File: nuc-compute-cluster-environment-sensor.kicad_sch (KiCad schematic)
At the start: 112 parts, among them J1 USB4105-GF-A, J2 SM04B-SRSS-TB-LF-SN, J3 SM04B-SRSS-TB-LF-SN, U1 FT4232H-56Q, U2 AP7370-33SA-7, U3 STM32G474CET6, U4 MB85RC1MTPNF-G, U5 SHT45, U6 BME280, Y1 ABM3B-12.000MHZ-B2-T, Y2 ECS-_327-12_5-34B-TR, Y3 ABM3B-8.000MHZ-10-1-U-T

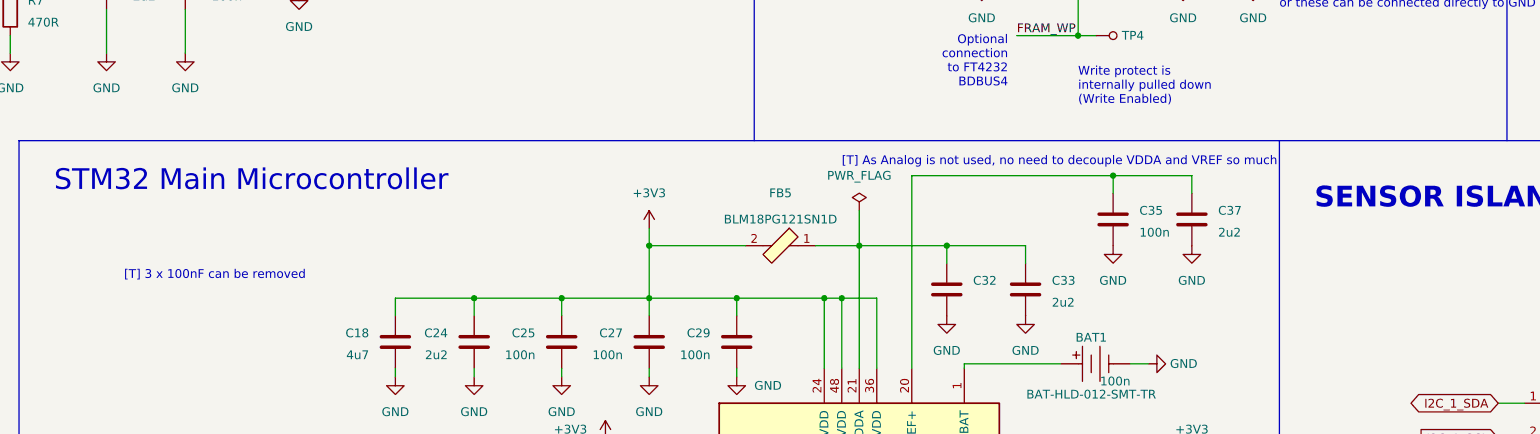
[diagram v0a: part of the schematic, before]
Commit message: Started to route signals to closest passive components to seek for possible placement optimization
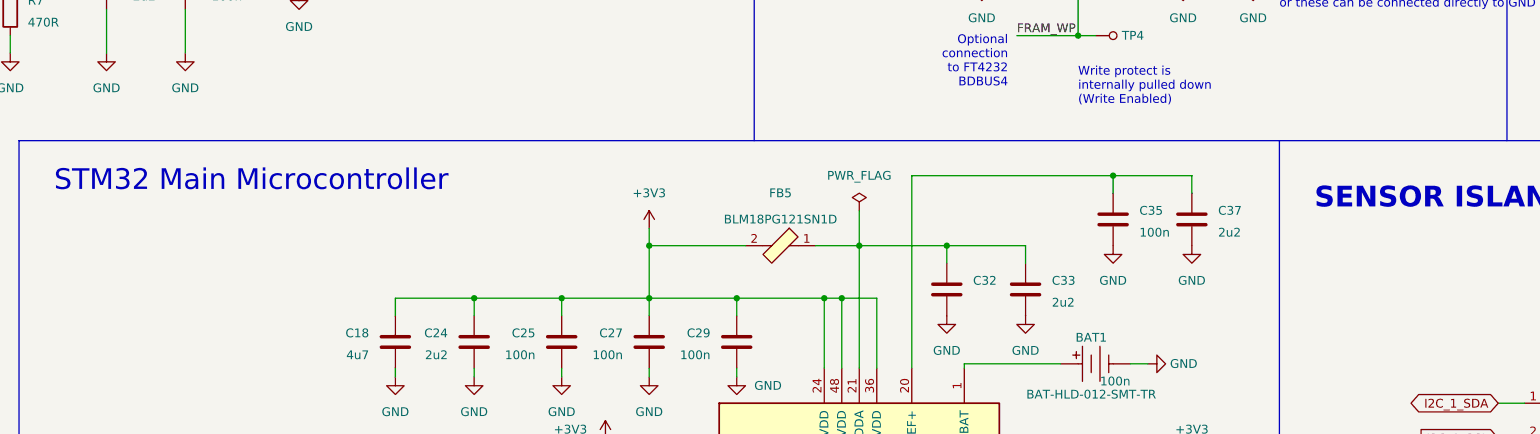
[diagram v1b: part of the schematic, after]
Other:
- note removed: "[T] 3 x 100nF can be removed"
- note removed: "[T] As Analog is not used, no need to decouple VDDA and VREF so much"

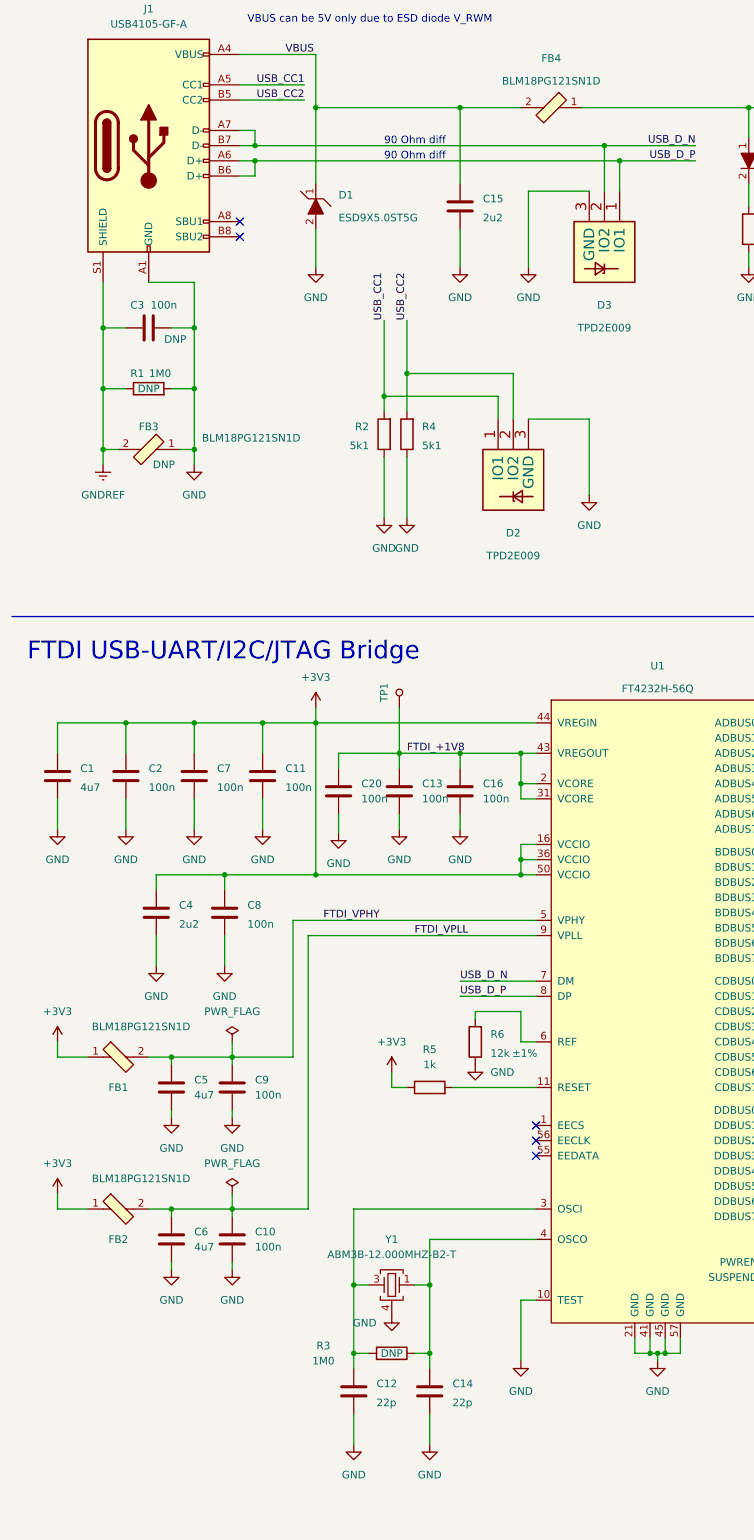
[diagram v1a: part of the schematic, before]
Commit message: Another iteration of component placements, initial routing of signals
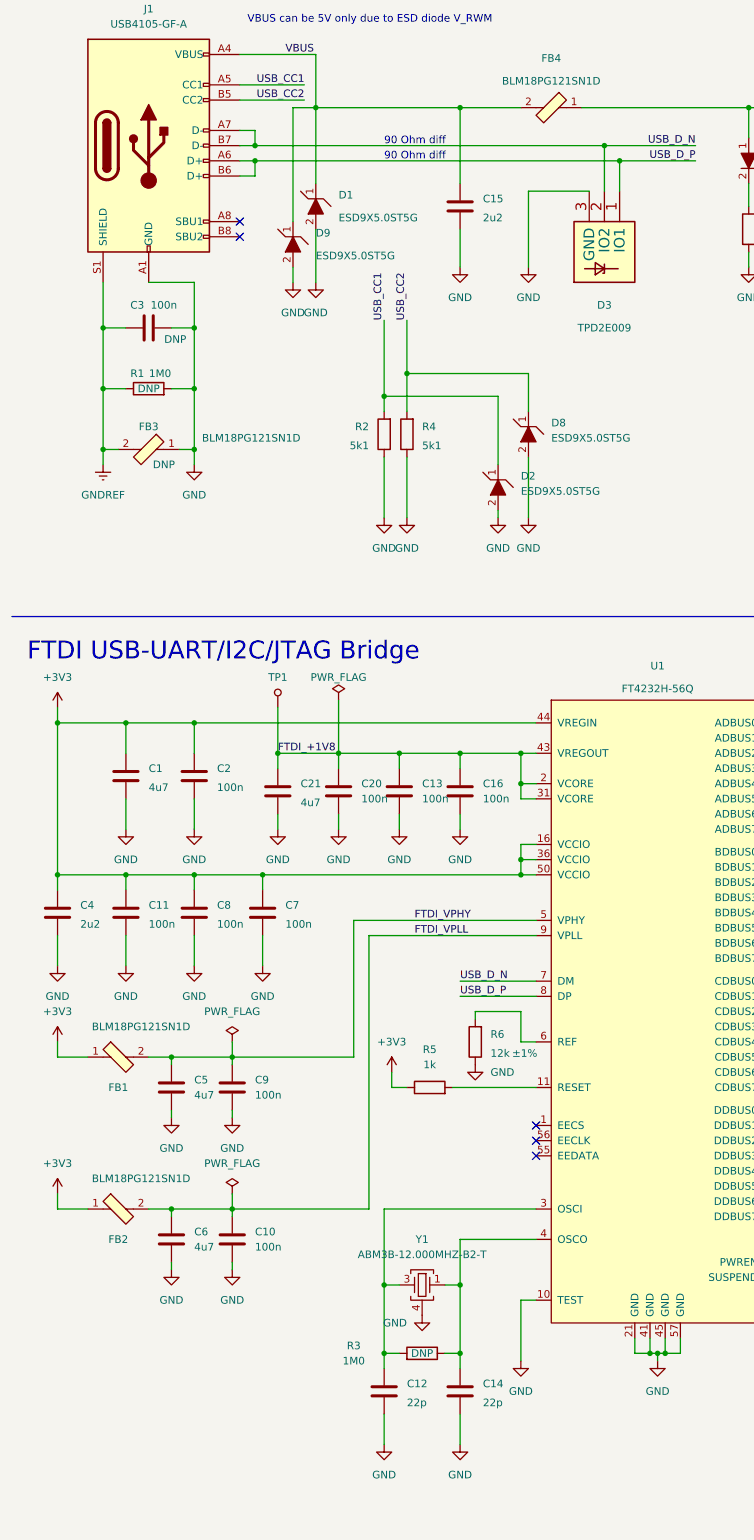
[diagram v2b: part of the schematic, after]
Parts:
- removed D2: TPD2E009, antmicro-footprints:SOT-723, symbol antmicroTVSDiodes:TPD2E009
- added C21: C_4u7_0402, antmicro-footprints:0402-cap, symbol antmicroCapacitors0402:C_4u7_0402
- added D2, D8, D9: ESD9X5.0ST5G, antmicro-footprints:SOD-923, symbol antmicroTVSDiodes:ESD9X5.0ST5G
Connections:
- net FTDI_+1V8: now also C21.1
- net GND: now also C21.2, D2.2, D8.2, D9.2
- net USB_CC1: now also D2.1
- net USB_CC2: now also D8.1
- net VBUS: now also D9.1
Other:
- moved on the sheet: C1, C11, C12, C14, C2, C4, C7, C8, R3, TP1, Y1

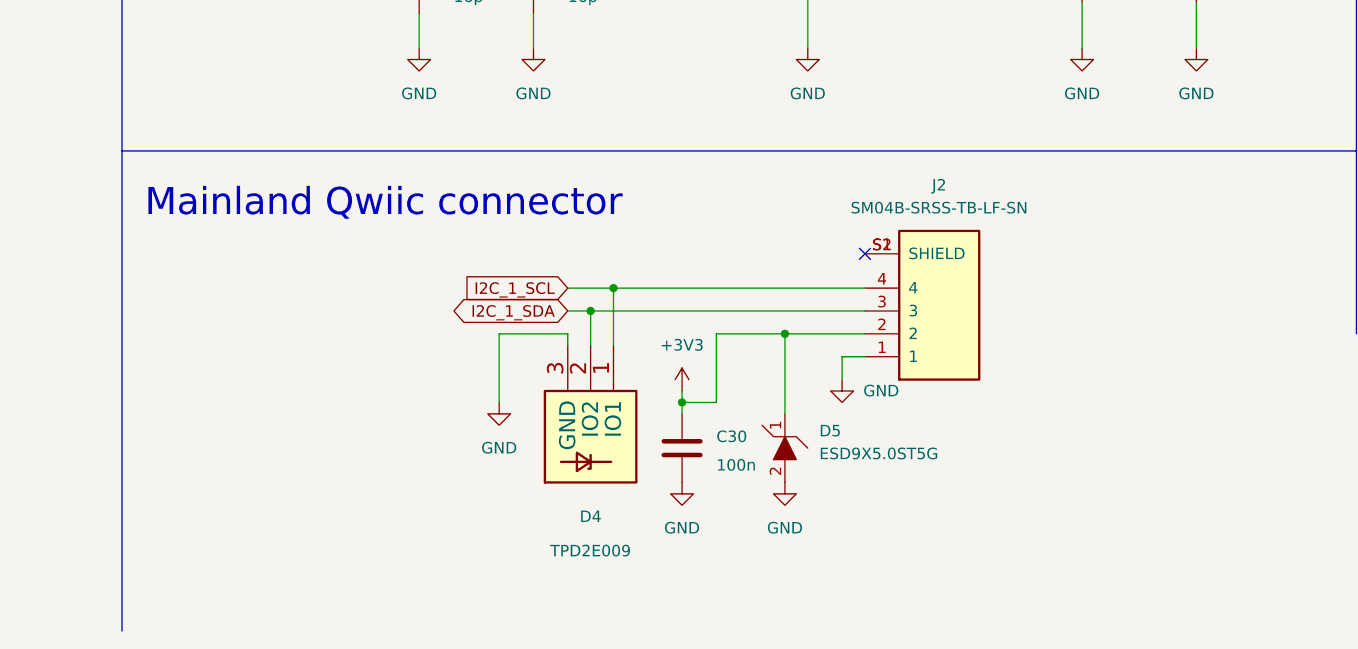
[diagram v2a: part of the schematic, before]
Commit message: Added mounting holes and changed PCB size to 50x30mm
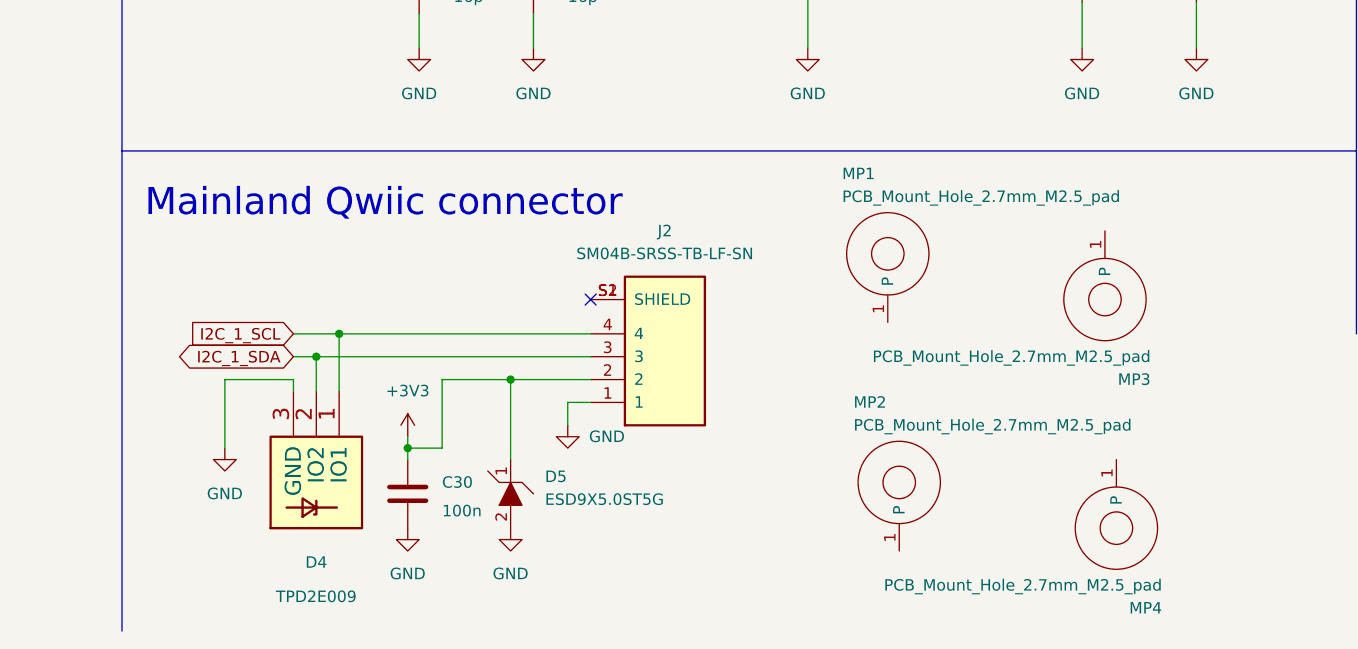
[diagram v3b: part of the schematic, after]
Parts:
- added MP1, MP2, MP3, MP4: PCB_Mount_Hole_2.7mm_M2.5_pad, antmicro-footprints:mounting-hole-2.7mm-M2.5-Pad, symbol antmicroMechanicalParts:PCB_Mount_Hole_2.7mm_M2.5_pad
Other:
- moved on the sheet: C30, D4, D5, J2

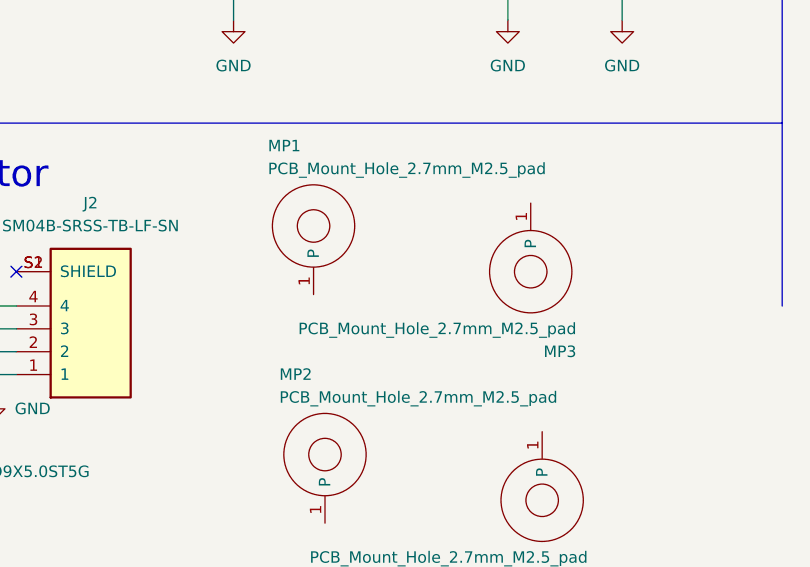
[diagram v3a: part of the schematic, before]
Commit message: New component placement after review, all components moved to top layer except battery and connector
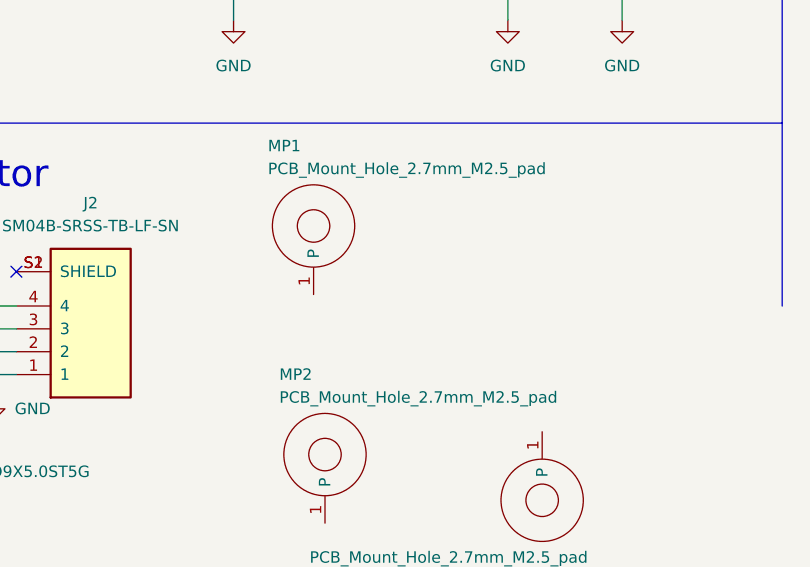
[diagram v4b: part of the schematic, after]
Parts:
- removed MP3: PCB_Mount_Hole_2.7mm_M2.5_pad, antmicro-footprints:mounting-hole-2.7mm-M2.5-Pad, symbol antmicroMechanicalParts:PCB_Mount_Hole_2.7mm_M2.5_pad

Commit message: Added 1k pullup on FRAM write protection pin, 470R serial resistors added on SWDIO and SWCLK, keepout zones for GND added around USB
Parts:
- added R10, R9: R_470R_0402, antmicro-footprints:0402-res, symbol antmicroResistors0402:R_470R_0402
- added R27: R_1k_0402, antmicro-footprints:0402-res, symbol antmicroResistors0402:R_100k_0402
- renumbered C4 to C1, C7 to C11, C21 to C12, C20 to C13, C12 to C14, C13 to C15, C15 to C16, C16 to C17, C14 to C18, C17 to C19, C1 to C2, C19 to C20, C18 to C21, C23 to C22, C24 to C23, C30 to C24, C11 to C3, C31 to C30, C32 to C31, C33 to C32, C34 to C33, C35 to C34, C36 to C35, C37 to C36, C38 to C37, C39 to C38, C40 to C39, C3 to C4, C41 to C40, C2 to C7, D9 to D1, D1 to D2, D2 to D3, D8 to D4, D3 to D5, D4 to D6, D5 to D7, D6 to D8, D7 to D9, MP4 to MP3, R9 to R11, R10 to R12, R11 to R13, R12 to R14, R13 to R15, R14 to R16, R15 to R17, R16 to R18, R17 to R19, R18 to R20, R19 to R21, R20 to R22, R21 to R23, R22 to R24, R23 to R25, R24 to R26, R25 to R28, R26 to R29, R4 to R3, R27 to R30, R28 to R31, R29 to R32, R30 to R33, R31 to R34, R32 to R35, R33 to R36, R34 to R37, R35 to R38, R36 to R39, R3 to R4, R37 to R40
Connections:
- net +3V3: now also R27.2
- net FRAM_WP: now also R27.1
- net SWCLK-JTCK: now also R9.1; no longer U1.12 (ADBUS0)
- net SWDIO-JTMS: now also R10.1; no longer U1.15 (ADBUS3)
- new net: R9.2, U1.12 (ADBUS0)
- new net: R10.2, U1.15 (ADBUS3)

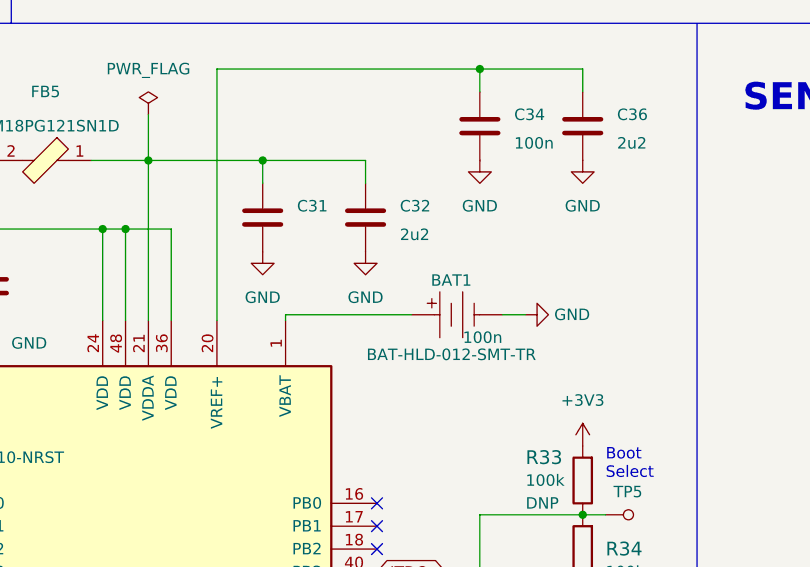
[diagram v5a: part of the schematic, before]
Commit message: Corrected MPN and values on schematic for C13 C15 C17
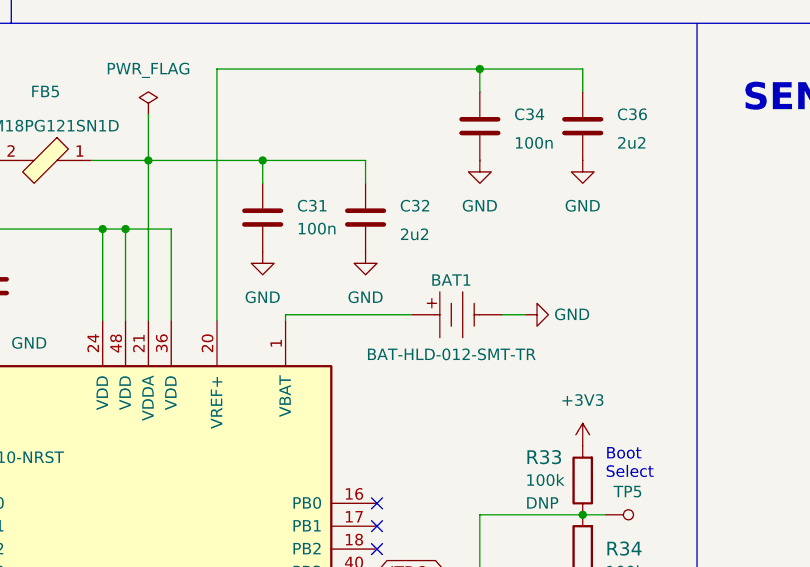
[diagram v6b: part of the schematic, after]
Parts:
- C13, C15: value C_4u7_0402 -> C_100n_0402; MPN GRM155R61A475MEAAD -> GRM155R61H104KE14D

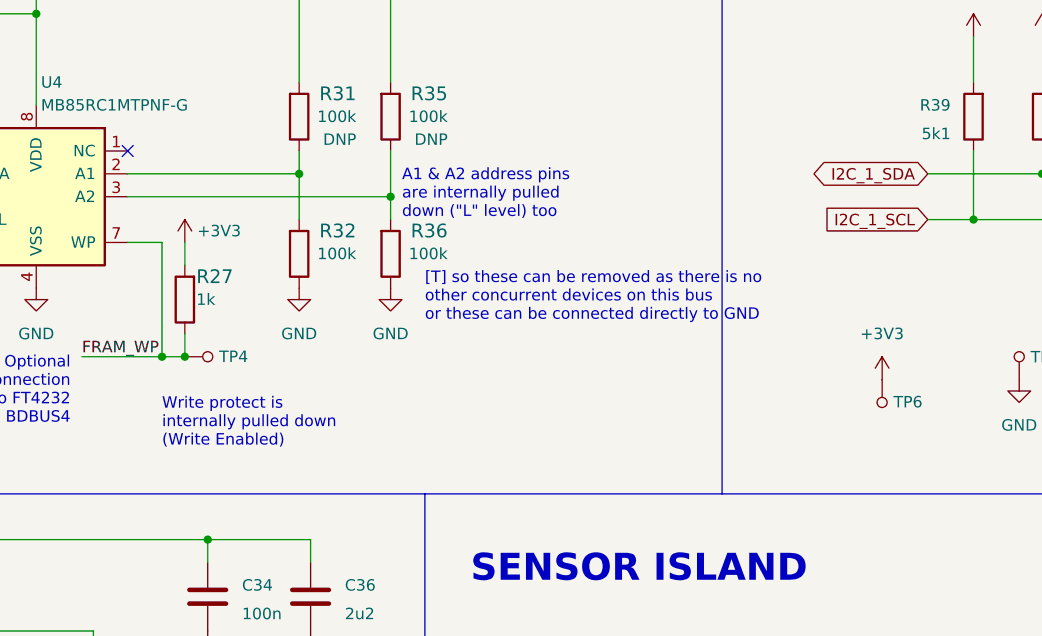
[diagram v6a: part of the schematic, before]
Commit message: Small tweaks on schematic comments and PCB silkscreen, exported wrl models, README finished
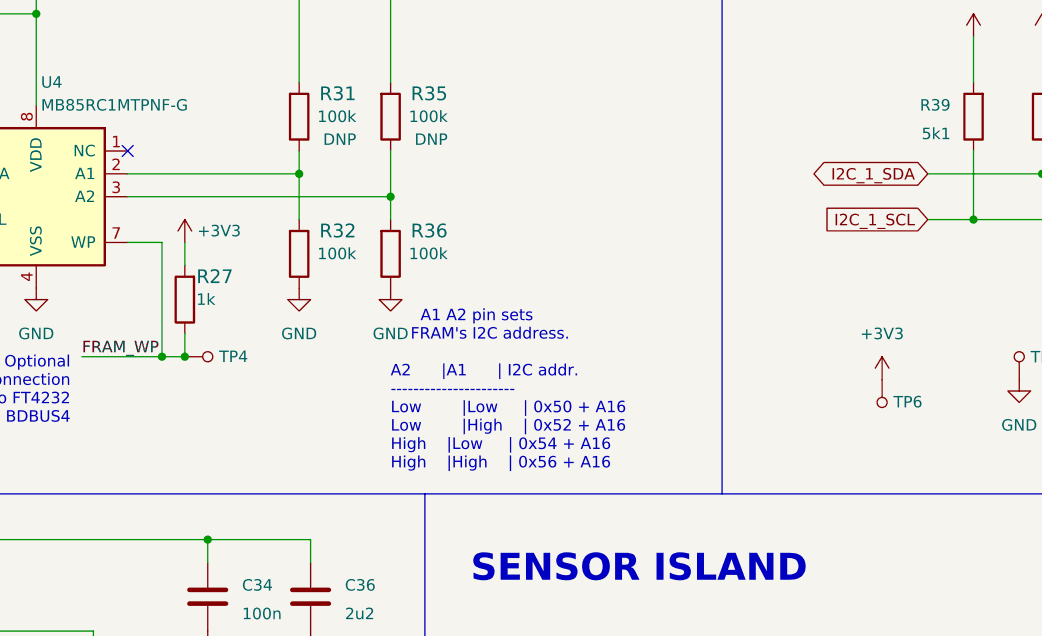
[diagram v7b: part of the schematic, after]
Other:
- note added: "A1 A2 pin sets FRAM's I2C address. A2 |A1 | I2C addr. ---------------------- Low |Low | 0x50 + A16 Low |High | 0x52 + A16 High |Low | 0x54 + A16 High |High | 0x56 + A16"
- note removed: "A1 & A2 address pins are internally pulled down ("L" level) too"
- note removed: "Write protect is internally pulled down (Write Enabled)"
- note removed: "[T] so these can be removed as there is no other concurrent devices on this bus or these can be connected directly to GND"
